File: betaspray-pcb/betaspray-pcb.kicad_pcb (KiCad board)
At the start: 2 copper layers, 30 parts, among them J1 USB_C_Receptacle_USB2.0_16P, J10 Conn_01x09_Pin, J11 Conn_01x03_Pin, J12 Conn_01x03_Pin, J13 Conn_01x03_Pin, J14 Conn_01x03_Pin, J15 Conn_01x03_Pin, J16 Conn_01x03_Pin, J17 Conn_01x03_Pin, J18 Conn_01x03_Pin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

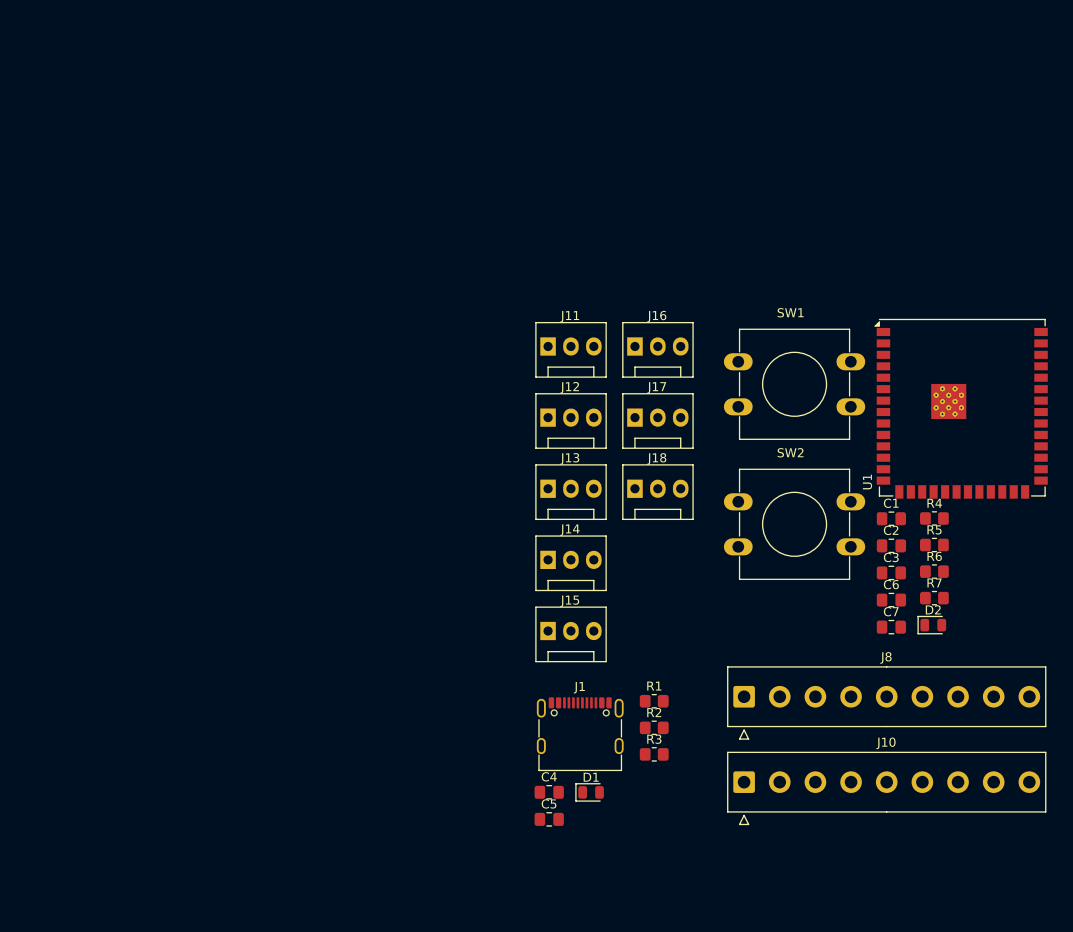
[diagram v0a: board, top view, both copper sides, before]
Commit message: 99.4mmx99.4mm layout
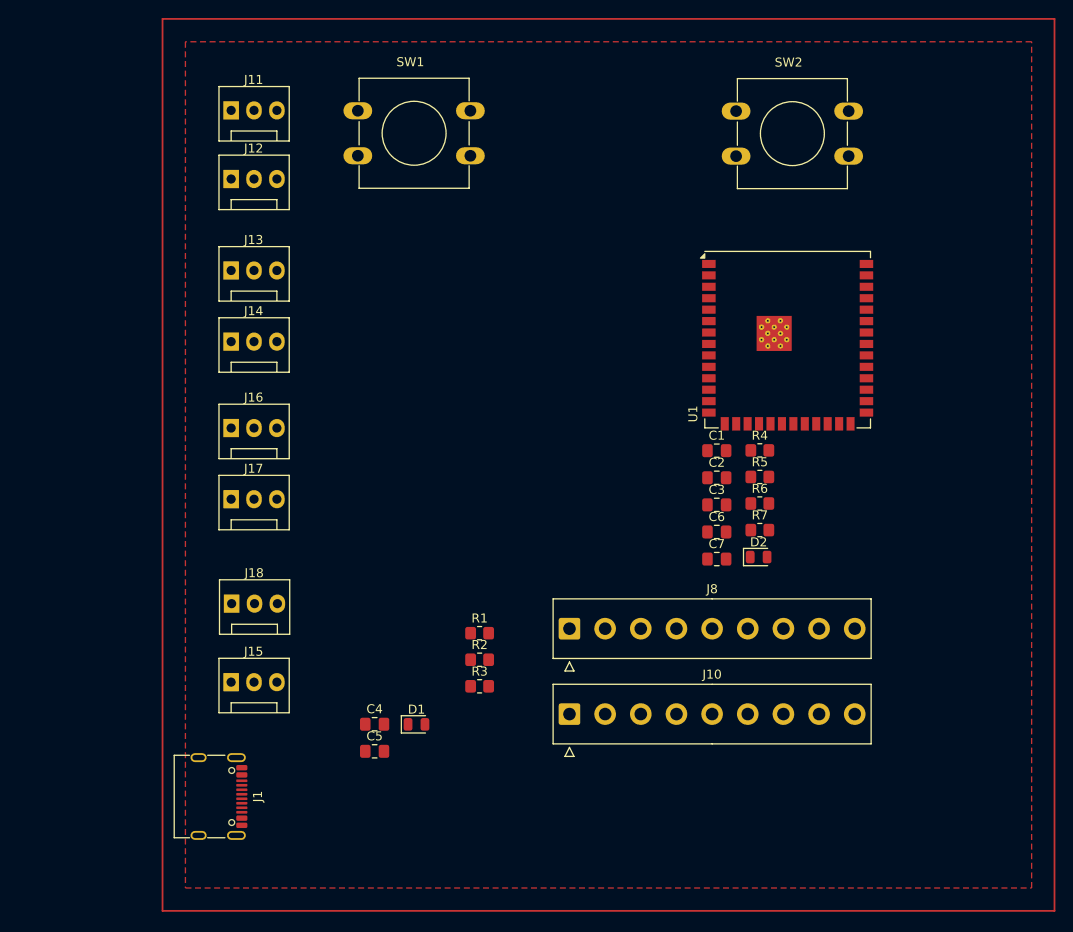
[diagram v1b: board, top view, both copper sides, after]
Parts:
- moved SW1 50.6 mm to (113.1, 48.3)
- moved J18 46.6 mm to (99.1, 103.0)
- moved J16 45.8 mm to (99.1, 83.5)
- moved J17 45.8 mm to (99.1, 91.4)
- moved J12 44.1 mm to (99.1, 55.9)
- moved J11 43.9 mm to (99.1, 48.3)
- moved SW2 43.4 mm to (155.1, 48.3)
- moved J14 42.7 mm to (99.1, 73.9)
- moved J13 42.7 mm to (99.1, 66.0)
- moved J1 41.8 mm to (96.5, 124.5), turned to -90 degrees
- moved J15 35.7 mm to (99.1, 111.8)
- moved J8 20.8 mm to (136.6, 105.8)
- moved R1 20.8 mm to (126.7, 106.3)
- moved R2 20.8 mm to (126.7, 109.3)
- moved R3 20.8 mm to (126.7, 112.2)
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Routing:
- added copper zone on F.Cu, net GND

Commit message: Trying to route
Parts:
- added U2: LM3940IT-3.3, LDO:TO254P1054X470X1955-3, F.Cu at (119.4, 83.8)
- SW1, SW2: footprint Button_Switch_THT:SW_PUSH-12mm -> Button_Switch_SMD:SW_DIP_SPSTx02_Slide_9.78x7.26mm_W8.61mm_P2.54mm
- moved J10 80.2 mm to (101.6, 43.2), turned to -90 degrees
- moved D1 52.1 mm to (158.0, 81.2), turned to 90 degrees
- moved J11 51.8 mm to (109.2, 99.1)
- moved J12 51.8 mm to (109.2, 106.7)
- moved R3 46.4 mm to (161.0, 81.0), turned to -90 degrees
- moved J15 42.3 mm to (119.4, 74.6)
- moved J18 41.1 mm to (116.9, 66.0)
- moved J1 38.2 mm to (99.1, 86.4)
- moved C6 36.8 mm to (139.0, 61.0)
- moved C7 36.1 mm to (155.0, 62.0)
- moved J8 35.6 mm to (101.6, 99.6), turned to -90 degrees
- moved R4 33.9 mm to (134.9, 61.0)
- moved R7 32.5 mm to (141.0, 67.0)
- moved D2 32.5 mm to (140.9, 70.0)
- moved R2 31.4 mm to (108.2, 83.8)
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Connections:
- C3 pad 1: VDD33 -> (no net)
- C3 pad 2: GND -> (no net)
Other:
- board outline added: 76.2 x 99.1 mm

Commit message: Trying to route
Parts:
- moved J10 88.1 mm to (99.6, 131.3), turned to 90 degrees
- moved SW2 71.3 mm to (134.6, 121.9), turned to 180 degrees
- moved C7 54.6 mm to (138.3, 114.0)
- moved R5 49.7 mm to (138.3, 110.3), turned to 180 degrees
- moved J11 49.6 mm to (97.8, 50.8)
- moved J12 49.6 mm to (97.8, 58.4)
- moved J16 49.6 mm to (108.0, 50.8)
- moved J17 49.6 mm to (108.0, 58.7)
- moved J8 32.6 mm to (109.2, 131.2), turned to 90 degrees
- moved J18 21.1 mm to (97.8, 75.0)
- moved R4 15.0 mm to (149.4, 65.0)
- moved SW1 13.9 mm to (150.6, 53.0)
- moved J13 11.4 mm to (97.8, 66.3)
- moved J15 11.4 mm to (108.0, 74.9)
- moved C6 10.4 mm to (149.4, 61.3), turned to 180 degrees
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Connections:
- C3 pad 1: (no net) -> VDD33
- C3 pad 2: (no net) -> GND
- C5 pad 1: VDD3V -> VDD33
- D1 pad 2: VDD3V -> VDD33
- J11 pad 2: VDD5 -> VDD5V
- J12 pad 2: VDD5 -> VDD5V
- J13 pad 2: VDD5 -> VDD5V
- J14 pad 2: VDD5 -> VDD5V
- J15 pad 2: VDD5 -> VDD5V
- J16 pad 2: VDD5 -> VDD5V
- J17 pad 2: VDD5 -> VDD5V
- J18 pad 2: VDD5 -> VDD5V
- U1 pad 12: /SERV7 -> /SERV5
- U1 pad 17: D2 -> /SERV6
- U1 pad 18: D3 -> /SERV7
- U1 pad 23: VS_SYNC_ROW -> D3
- U1 pad 24: CAM_PWR_DEL -> D2
- U1 pad 28: PIXEL_CLK -> CAM_PWR_DEL
- U1 pad 31: SCL -> VS_SYNC_FRAME
- U1 pad 33: VS_SYNC_FRAME -> SCL
- U1 pad 38: /SERV1 -> VS_SYNC_ROW
- U1 pad 39: /SERV0 -> PIXEL_CLK
- U1 pad 4: /SERV3 -> /SERV0
- U1 pad 5: /SERV4 -> /SERV1
- U1 pad 6: /SERV5 -> /SERV4
- U1 pad 7: /SERV6 -> /SERV3
- U2 pad 3: VDD3V -> VDD33
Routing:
- net /EN: track 0.00 -> 29.3 mm
- net /BOOT: track 0.00 -> 27.4 mm
- net Net-(D2-K): track 0.00 -> 7.87 mm
- net Net-(J1-CC1): track 0.00 -> 4.97 mm
- net Net-(J1-CC2): track 0.00 -> 4.22 mm
- net VDD33: track 0.00 -> 3.28 mm
- net Net-(D1-K): track 0.00 -> 2.04 mm
- added copper zone on In2.Cu, net GND
- added copper zone on In1.Cu, net VDD33
- added copper zone on In1.Cu, net VDD5V
- removed copper zone on F.Cu, net GND
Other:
- copper layers 2 -> 4

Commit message: Routed
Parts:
- moved J10 15.5 mm to (115.1, 131.3)
- moved J8 5.09 mm to (104.1, 131.6)
- moved R6 4.83 mm to (128.3, 79.2)
- moved C5 4.58 mm to (128.3, 86.4), turned to -90 degrees
- moved R7 2.39 mm to (143.4, 70.9)
- moved D2 2.39 mm to (143.3, 73.9)
- moved C4 2.31 mm to (118.1, 88.9)
- moved R5 1.67 mm to (138.2, 108.6)
- moved SW2 1.67 mm to (134.5, 120.3)
- moved C7 1.67 mm to (138.1, 112.3)
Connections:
- U1 pad 10: /SERV2 -> Net-(D2-K)
- U1 pad 11: Net-(D2-K) -> /SERV2
- U1 pad 12: /SERV5 -> /SERV3
- U1 pad 17: /SERV6 -> /SERV4
- U1 pad 19: D4 -> CAM_PWR_DEL
- U1 pad 20: D5 -> D2
- U1 pad 21: D6 -> D4
- U1 pad 22: D7 -> D6
- U1 pad 23: D3 -> D8
- U1 pad 24: D2 -> VS_SYNC_ROW
- U1 pad 25: CAM_RST -> SDA
- U1 pad 26: unconnected-(U1-IO45-Pad26) -> CAM_RST
- U1 pad 28: CAM_PWR_DEL -> unconnected-(U1-IO35-Pad28)
- U1 pad 31: VS_SYNC_FRAME -> D3
- U1 pad 32: SDA -> D5
- U1 pad 33: SCL -> D7
- U1 pad 34: unconnected-(U1-IO41-Pad34) -> D9
- U1 pad 35: unconnected-(U1-IO42-Pad35) -> PIXEL_CLK
- U1 pad 38: VS_SYNC_ROW -> VS_SYNC_FRAME
- U1 pad 39: PIXEL_CLK -> SCL
- U1 pad 5: /SERV1 -> /SERV5
- U1 pad 6: /SERV4 -> /SERV1
- U1 pad 7: /SERV3 -> /SERV6
- U1 pad 8: D8 -> unconnected-(U1-IO15-Pad8)
- U1 pad 9: D9 -> unconnected-(U1-IO16-Pad9)
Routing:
- net /SERV0: track 0.00 -> 66.7 mm
- net /SERV1: track 0.00 -> 61.6 mm
- net SDA: track 0.00 -> 61.4 mm
- net SCL: track 0.00 -> 58.8 mm
- net VS_SYNC_ROW: track 0.00 -> 58.6 mm
- net /USB_D_N: track 0.00 -> 57.6 mm
- net /SERV5: track 0.00 -> 55.3 mm
- net VDD33: track 3.28 -> 57.9 mm, vias 0 -> 2
- net VS_SYNC_FRAME: track 0.00 -> 53.9 mm
- net /USB_D_P: track 0.00 -> 52.3 mm
- net D8: track 0.00 -> 51.8 mm
- net /SERV6: track 0.00 -> 50.8 mm
- net D6: track 0.00 -> 48.8 mm
- net PIXEL_CLK: track 0.00 -> 46.5 mm
- net D4: track 0.00 -> 45.7 mm
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
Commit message: Stiched the planes
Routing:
- net GND: track 0.00 -> 37.7 mm, vias 0 -> 16
- net VDD33: track 57.9 -> 72.2 mm, vias 2 -> 9

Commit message: Added lasers to schematic and footprint
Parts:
- removed D2: LED, LED_SMD:LED_0805_2012Metric
- removed R7: 300, Resistor_SMD:R_0805_2012Metric_Pad1.20x1.40mm_HandSolder
- added J2: Conn_01x02, Connector_PinHeader_2.54mm:PinHeader_2x01_P2.54mm_Vertical, F.Cu at (119.7, 62.9)
- added J3: Conn_01x02, Connector_PinHeader_2.54mm:PinHeader_2x01_P2.54mm_Vertical, F.Cu at (119.7, 45.8)
- added J4: Conn_01x02, Connector_PinHeader_2.54mm:PinHeader_2x01_P2.54mm_Vertical, F.Cu at (119.7, 53.7)
- added J5: Conn_01x02, Connector_PinHeader_2.54mm:PinHeader_2x01_P2.54mm_Vertical, F.Cu at (119.9, 71.1)
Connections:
- U1 pad 10: Net-(D2-K) -> /LSR_1
- U1 pad 15: unconnected-(U1-IO3-Pad15) -> /LSR_4
- U1 pad 8: unconnected-(U1-IO15-Pad8) -> /LSR_2
- U1 pad 9: unconnected-(U1-IO16-Pad9) -> /LSR_3
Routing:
- net /LSR_2: track 0.00 -> 45.4 mm, vias 0 -> 2
- net /LSR_3: track 0.00 -> 40.7 mm, vias 0 -> 2
- net /LSR_1: track 0.00 -> 27.6 mm
- net /LSR_4: track 0.00 -> 19.2 mm, vias 0 -> 2
- net GND: track 37.7 -> 45.3 mm, vias 16 -> 19
- net Net-(D2-K): track 5.14 -> 0.00 mm
- net Net-(D2-A): track 3.74 -> 0.00 mm
- net VDD33: track 72.2 -> 70.1 mm, vias 9 -> 8

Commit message: Ver0, pls'
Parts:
- removed J1: USB_C_Receptacle_USB2.0_16P, Connector_USB:USB_C_Receptacle_G-Switch_GT-USB-7010ASV
- added C10: 2200uF, Capacitor_THT:CP_Radial_D16.0mm_P7.50mm, F.Cu at (130.2, 63.5)
- added C11: 2200uF, Capacitor_THT:CP_Radial_D16.0mm_P7.50mm, F.Cu at (129.9, 46.2)
- added C8: 0.1 uF, Capacitor_SMD:C_0805_2012Metric_Pad1.18x1.45mm_HandSolder, F.Cu at (125.9, 88.1)
- added C9: 100 uF, Capacitor_SMD:C_0805_2012Metric_Pad1.18x1.45mm_HandSolder, F.Cu at (123.4, 88.1)
- added H1: MountingHole, MountingHole:MountingHole_3.2mm_M3, F.Cu at (81.8, 44.5)
- added H2: MountingHole, MountingHole:MountingHole_3.2mm_M3, F.Cu at (168.5, 44.5)
- added H3: MountingHole, MountingHole:MountingHole_3.2mm_M3, F.Cu at (81.8, 131.0)
- added H4: MountingHole, MountingHole:MountingHole_3.2mm_M3, F.Cu at (168.4, 131.1)
- added Q1: AO3400A, Package_TO_SOT_SMD:SOT-23, F.Cu at (118.4, 72.3)
- added R7: 300, Resistor_SMD:R_0805_2012Metric_Pad1.20x1.40mm_HandSolder, F.Cu at (124.7, 73.3)
- added R8: 10K, Resistor_SMD:R_0805_2012Metric_Pad1.20x1.40mm_HandSolder, F.Cu at (121.7, 72.2)
- added e1: USB_C_Receptacle_USB2.0_16P, Connector_USB:USB_C_Receptacle_G-Switch_GT-USB-7010ASV, F.Cu at (99.0, 86.4)
- moved J5 2.53 mm to (119.6, 68.6)
- moved J2 1.05 mm to (119.8, 61.8)
- moved R6 0.89 mm to (128.3, 80.1)
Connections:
- J2 pad 1: GND -> Net-(J2-Pin_1)
- J2 pad 2: /LSR_1 -> VDD5V
- J3 pad 1: GND -> Net-(J2-Pin_1)
- J3 pad 2: /LSR_2 -> VDD5V
- J4 pad 1: GND -> Net-(J2-Pin_1)
- J4 pad 2: /LSR_3 -> VDD5V
- J5 pad 1: GND -> Net-(J2-Pin_1)
- J5 pad 2: /LSR_4 -> VDD5V
- U1 pad 15: /LSR_4 -> unconnected-(U1-IO3-Pad15)
- U1 pad 8: /LSR_2 -> unconnected-(U1-IO15-Pad8)
- U1 pad 9: /LSR_3 -> unconnected-(U1-IO16-Pad9)
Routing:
- net VDD5V: track 22.2 -> 147.8 mm, vias 1 -> 3
- net GND: track 45.3 -> 144.6 mm, vias 19 -> 18
- net /LSR_2: track 45.4 -> 0.00 mm, vias 2 -> 0
- net /LSR_3: track 40.7 -> 0.00 mm, vias 2 -> 0
- net Net-(J2-Pin_1): track 0.00 -> 27.9 mm, vias 0 -> 1
- net /LSR_4: track 19.2 -> 0.00 mm, vias 2 -> 0
- net /USB_D_N: track 57.6 -> 46.8 mm
- net /SERV5: track 55.3 -> 47.6 mm
- net /LSR_1: track 27.6 -> 20.3 mm, vias 0 -> 2
- net /SERV0: track 66.7 -> 60.4 mm
- net /USB_D_P: track 52.3 -> 46.8 mm
- net Net-(Q1-G): track 0.00 -> 4.38 mm
- net VDD33: track 70.1 -> 74.3 mm
- net /SERV6: track 50.8 -> 49.3 mm, vias 0 -> 2
- net /SERV1: track 61.6 -> 61.2 mm, vias 0 -> 2
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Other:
- board size 76.2 x 99.1 mm -> 99.3 x 99.3 mm
- board text added: "ECE445 Team 41 Rev0 BetaSpray :)"
